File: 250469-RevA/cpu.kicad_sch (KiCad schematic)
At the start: 6 parts, among them J6 Conn_02x22_Edge_Female, U3 74LS08, U6 8500

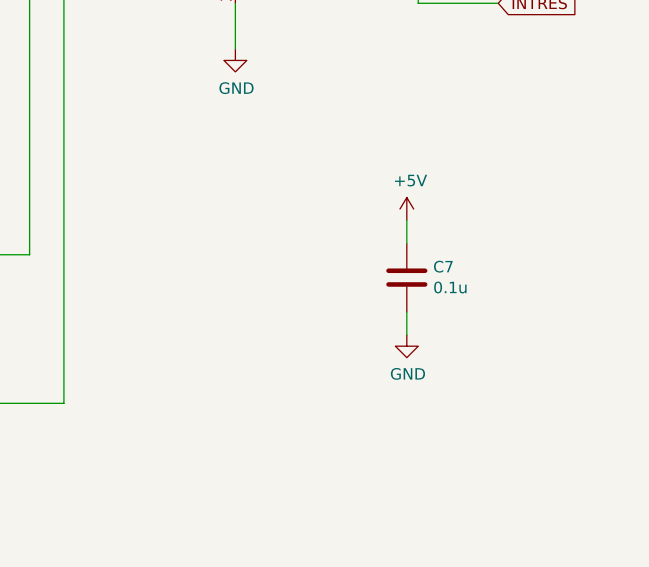
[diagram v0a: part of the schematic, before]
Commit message: Footprints and Symbols updates
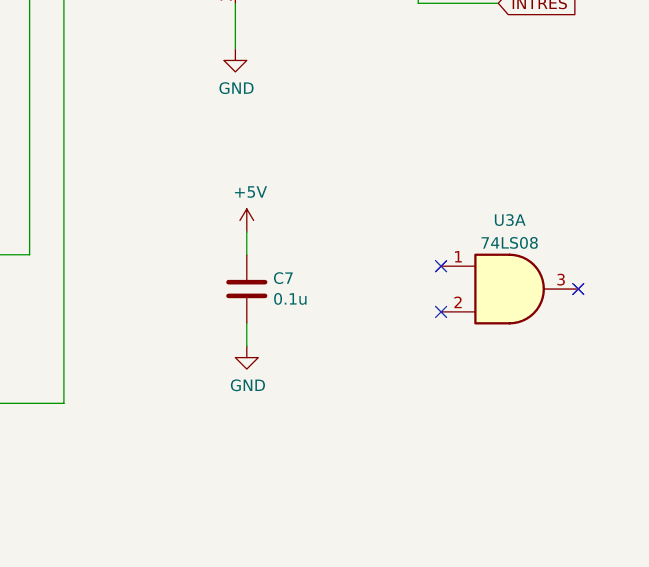
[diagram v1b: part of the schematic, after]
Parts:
- added unit 1 of U3
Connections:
- no-connect marks 1 -> 4
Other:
- moved on the sheet: C7
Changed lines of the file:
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@@
   (junction (at 146.05 138.43) (diameter 0) (color 0 0 0 0)
   )
+  (no_connect (at 256.54 142.24))
+  (no_connect (at 256.54 137.16))
+  (no_connect (at 271.78 139.7))
   (no_connect (at 44.45 173.99))
   (bus_entry (at 256.54 74.93) (size 2.54 -2.54)
@@
     (stroke (width 0) (type default))
   )
-  (wire (pts (xy 252.73 134.62) (xy 252.73 132.08))
+  (wire (pts (xy 234.95 135.89) (xy 234.95 133.35))
     (stroke (width 0) (type default))
   )
@@
     (stroke (width 0) (type default))
   )
-  (wire (pts (xy 252.73 142.24) (xy 252.73 144.78))
+  (wire (pts (xy 234.95 143.51) (xy 234.95 146.05))
     (stroke (width 0) (type default))
   )
@@
     )
   )
-  (symbol (lib_id "power:+5V") (at 252.73 132.08 0) (unit 1)
+  (symbol (lib_id "power:+5V") (at 234.95 133.35 0) (unit 1)
     (in_bom yes) (on_board yes) (dnp no)
-    (property "Reference" "#PWR0157" (at 252.73 135.89 0)
-      (effects (font (size 1.27 1.27)) hide)
-    )
-    (property "Value" "+5V" (at 253.111 127.6858 0)
-      (effects (font (size 1.27 1.27)))
-    )
-    (property "Footprint" "" (at 252.73 132.08 0)
-      (effects (font (size 1.27 1.27)) hide)
-    )
-    (property "Datasheet" "" (at 252.73 132.08 0)
+    (property "Reference" "#PWR0157" (at 234.95 137.16 0)
+      (effects (font (size 1.27 1.27)) hide)
+    )
+    (property "Value" "+5V" (at 235.331 128.9558 0)
+      (effects (font (size 1.27 1.27)))
+    )
+    (property "Footprint" "" (at 234.95 133.35 0)
+      (effects (font (size 1.27 1.27)) hide)
+    )
+    (property "Datasheet" "" (at 234.95 133.35 0)
       (effects (font (size 1.27 1.27)) hide)
     )
@@
     )
   )
-  (symbol (lib_id "power:GND") (at 252.73 144.78 0) (unit 1)
+  (symbol (lib_id "power:GND") (at 234.95 146.05 0) (unit 1)
     (in_bom yes) (on_board yes) (dnp no)
-    (property "Reference" "#PWR0158" (at 252.73 151.13 0)
-      (effects (font (size 1.27 1.27)) hide)
-    )
-    (property "Value" "GND" (at 252.857 149.1742 0)
-      (effects (font (size 1.27 1.27)))
-    )
-    (property "Footprint" "" (at 252.73 144.78 0)
-      (effects (font (size 1.27 1.27)) hide)
-    )
-    (property "Datasheet" "" (at 252.73 144.78 0)
+    (property "Reference" "#PWR0158" (at 234.95 152.4 0)
+      (effects (font (size 1.27 1.27)) hide)
+    )
+    (property "Value" "GND" (at 235.077 150.4442 0)
+      (effects (font (size 1.27 1.27)))
+    )
+    (property "Footprint" "" (at 234.95 146.05 0)
+      (effects (font (size 1.27 1.27)) hide)
+    )
+    (property "Datasheet" "" (at 234.95 146.05 0)
       (effects (font (size 1.27 1.27)) hide)
     )
@@
     )
   )
-  (symbol (lib_id "Device:C") (at 252.73 138.43 0) (unit 1)
+  (symbol (lib_id "Device:C") (at 234.95 139.7 0) (unit 1)
     (in_bom yes) (on_board yes) (dnp no)
-    (property "Reference" "C7" (at 255.651 137.2616 0)
+    (property "Reference" "C7" (at 237.871 138.5316 0)
       (effects (font (size 1.27 1.27)) (justify left))
     )
-    (property "Value" "0.1u" (at 255.651 139.573 0)
+    (property "Value" "0.1u" (at 237.871 140.843 0)
       (effects (font (size 1.27 1.27)) (justify left))
     )
-    (property "Footprint" "Capacitor_THT:C_Disc_D4.7mm_W2.5mm_P5.00mm" (at 253.6952 142.24 0)
-      (effects (font (size 1.27 1.27)) hide)
-    )
-    (property "Datasheet" "~" (at 252.73 138.43 0)
+    (property "Footprint" "Capacitor_THT:C_Disc_D4.7mm_W2.5mm_P5.00mm" (at 235.9152 143.51 0)
+      (effects (font (size 1.27 1.27)) hide)
+    )
+    (property "Datasheet" "~" (at 234.95 139.7 0)
       (effects (font (size 1.27 1.27)) hide)
     )
@@
         )
       )
+    )
+  )
+  (symbol (lib_id "74xx:74LS08") (at 264.16 139.7 0) (unit 1)
+    (in_bom yes) (on_board yes) (dnp no) (fields_autoplaced)
+    (property "Reference" "U3" (at 264.1517 132.08 0)
+      (effects (font (size 1.27 1.27)))
+    )
+    (property "Value" "74LS08" (at 264.1517 134.62 0)
+      (effects (font (size 1.27 1.27)))
+    )
+    (property "Footprint" "Package_DIP:DIP-14_W7.62mm_Socket" (at 264.16 139.7 0)
+      (effects (font (size 1.27 1.27)) hide)
+    )
+    (property "Datasheet" "http://www.ti.com/lit/gpn/sn74LS08" (at 264.16 139.7 0)
+      (effects (font (size 1.27 1.27)) hide)
+    )
+    (pin "1")
+    (pin "2")
+    (pin "3")
+    (pin "4")
+    (pin "5")
+    (pin "6")
+    (pin "10")
+    (pin "8")
+    (pin "9")
+    (pin "11")
+    (pin "12")
+    (pin "13")
+    (pin "14")
+    (pin "7")
+    (instances
+      (project "C64C-250469-01-A"
+        (path "/ceb6c8ef-b249-4909-95e5-e7359667aee8/00000000-0000-0000-0000-00005e3675d1"
+          (reference "U3") (unit 1)
+        )
+      )

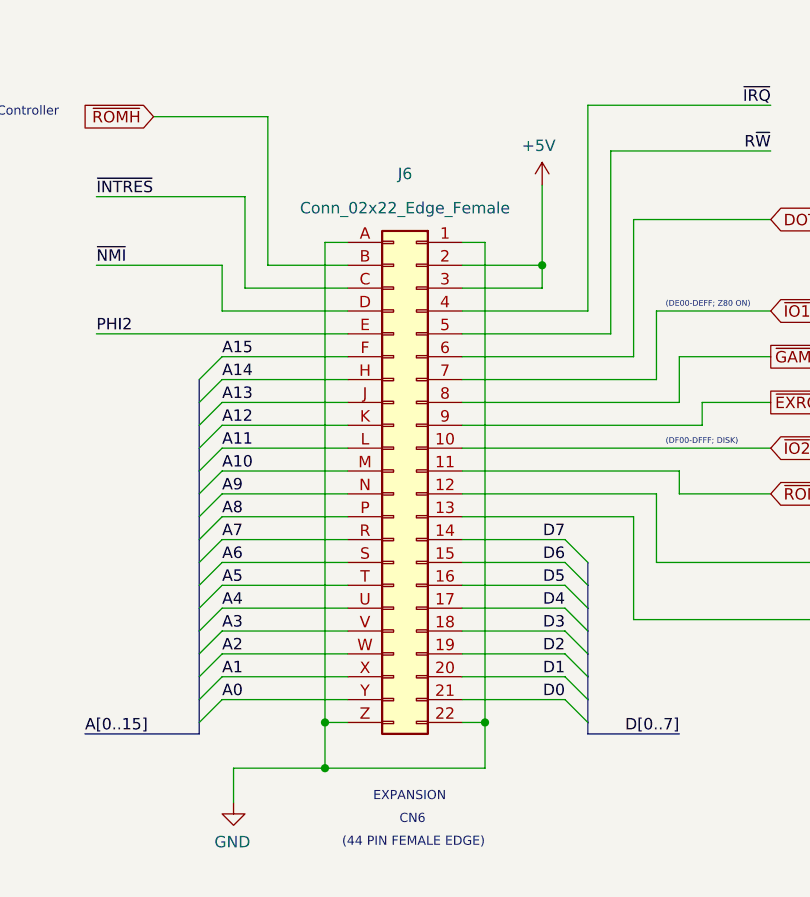
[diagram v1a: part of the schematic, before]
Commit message: Fixes after renaming the project library
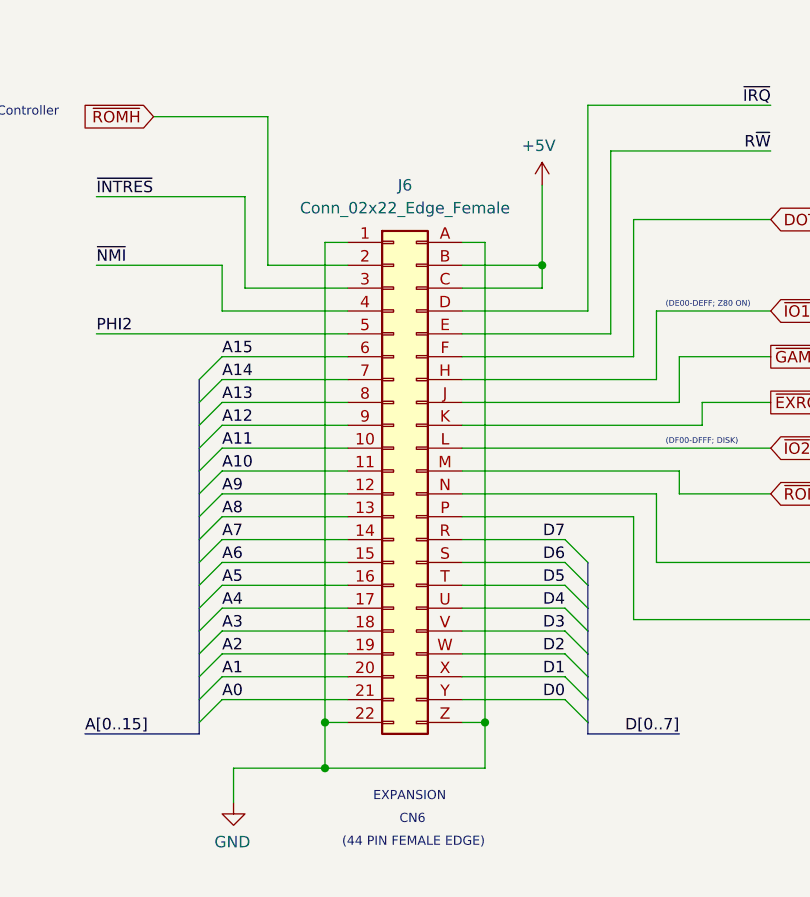
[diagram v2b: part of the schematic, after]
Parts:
- removed J6: Conn_02x22_Edge_Female, 250469-01:Sullins_EBC22DRAN, symbol 250469-01:Conn_02x22_Edge_Female
- added J6: Conn_02x22_Edge_Female, C64-C-250469:Sullins_EBC22DRAN, symbol C64-C-250469:Conn_02x22_Edge_Female
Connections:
- net +5V: now also J6.B (Pin_B), J6.C (Pin_C)
- net A0: now also J6.21 (Pin_21)
- net A1: now also J6.20 (Pin_20)
- net A10: now also J6.11 (Pin_11)
- net A11: now also J6.10 (Pin_10)
- net A12: now also J6.9 (Pin_9)
- net A13: now also J6.8 (Pin_8)
- net A14: now also J6.7 (Pin_7)
- net A15: now also J6.6 (Pin_6)
- net A2: now also J6.19 (Pin_19)
- net A3: now also J6.18 (Pin_18)
- net A4: now also J6.17 (Pin_17)
- net A5: now also J6.16 (Pin_16)
- net A6: now also J6.15 (Pin_15)
- net A7: now also J6.14 (Pin_14)
- net A8: now also J6.13 (Pin_13)
- net A9: now also J6.12 (Pin_12)
- net BA: now also J6.N (Pin_N)
- net D0: now also J6.Y (Pin_Y)
- net D1: now also J6.X (Pin_X)
- net D2: now also J6.W (Pin_W)
- net D3: now also J6.V (Pin_V)
- net D4: now also J6.U (Pin_U)
- net D5: now also J6.T (Pin_T)
- net D6: now also J6.S (Pin_S)
- net D7: now also J6.R (Pin_R)
- net DOTCLK: now also J6.F (Pin_F)
- net GND: now also J6.1 (Pin_1), J6.22 (Pin_22), J6.A (Pin_A), J6.Z (Pin_Z)
- net PHI2: now also J6.5 (Pin_5)
- net R~{W}: now also J6.E (Pin_E)
- net ~{DMA}: now also J6.P (Pin_P)
- net ~{EXROM}: now also J6.K (Pin_K)
- net ~{GAME}: now also J6.J (Pin_J)
- net ~{INTRES}: now also J6.3 (Pin_3)
- net ~{IO1}: now also J6.H (Pin_H)
- net ~{IO2}: now also J6.L (Pin_L)
- net ~{IRQ}: now also J6.D (Pin_D)
- net ~{NMI}: now also J6.4 (Pin_4)
- net ~{ROMH}: now also J6.2 (Pin_2)
- net ~{ROML}: now also J6.M (Pin_M)
